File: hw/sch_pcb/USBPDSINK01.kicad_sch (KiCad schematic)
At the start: 51 parts, among them J1 USBC_USB4105-GF-A, J11 WAGO_2604-3102, J2 HEADER_2x05_PARALLEL, J3 HEADER_2x04_PARALLEL, J4 HEADER_2x03_PARALLEL, J5 HEADER_2x01, J6 HEADER_2x07_PARALLEL, M1 HOLE, M2 HOLE, M3 HOLE, M4 HOLE, Q2 IRF7469PbF, U1 STUSB4500QTR, U2 NCP1117-3.3

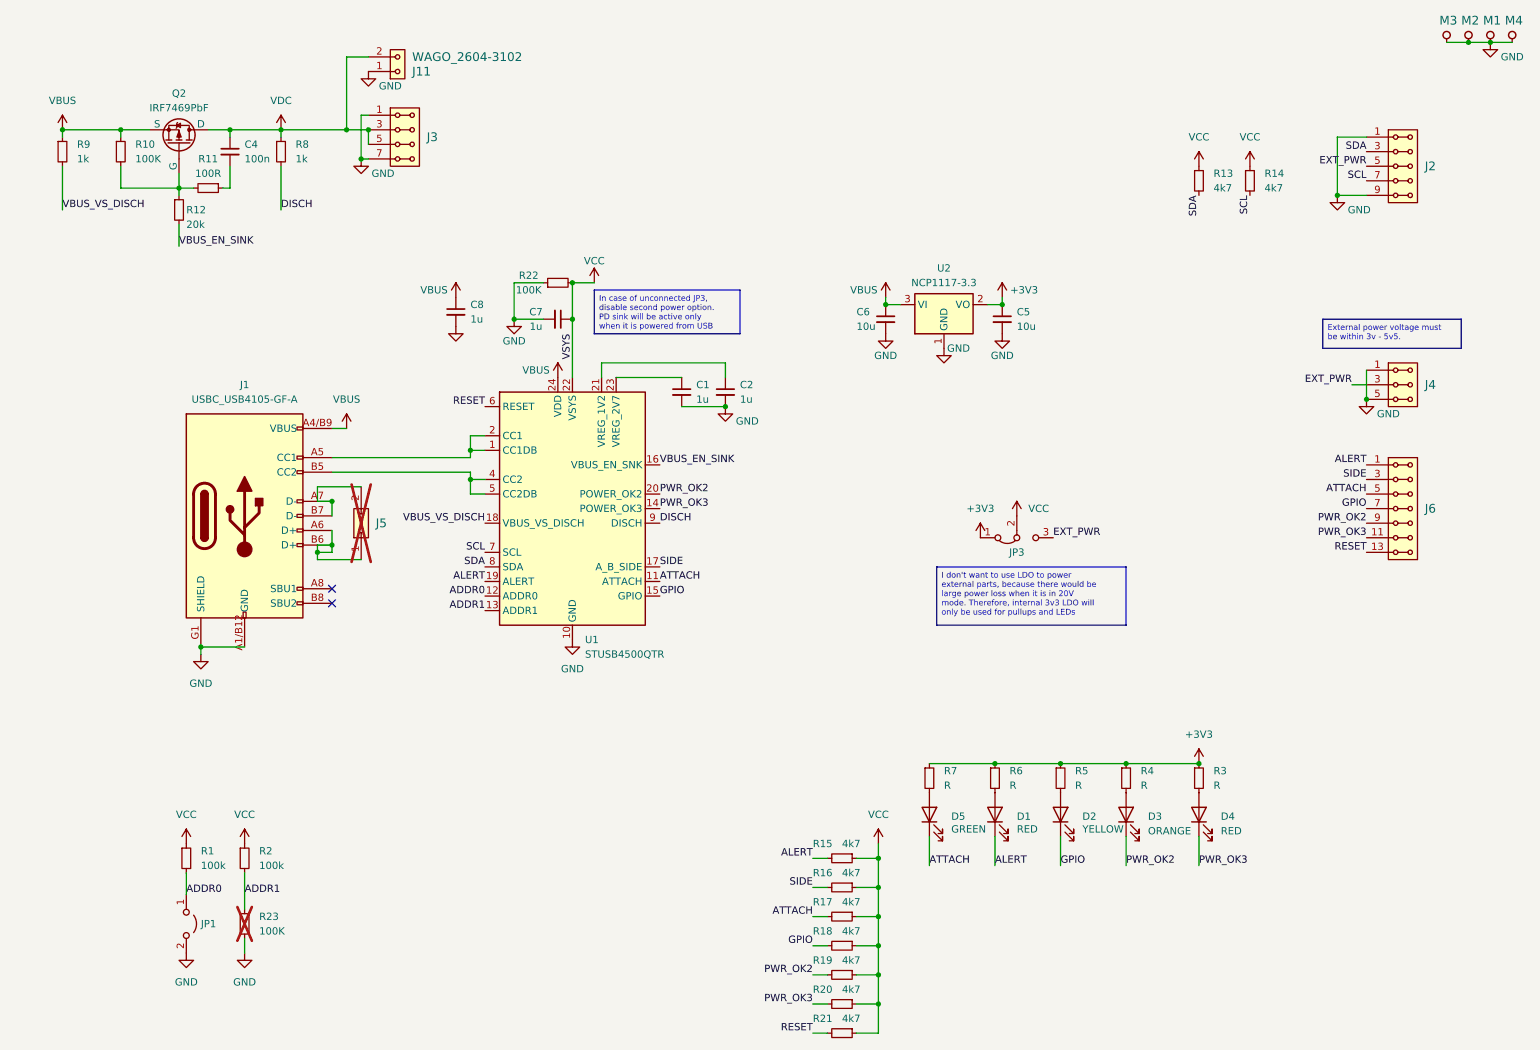
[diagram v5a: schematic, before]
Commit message: minor updates in layout, clean schematics, add components MFPN
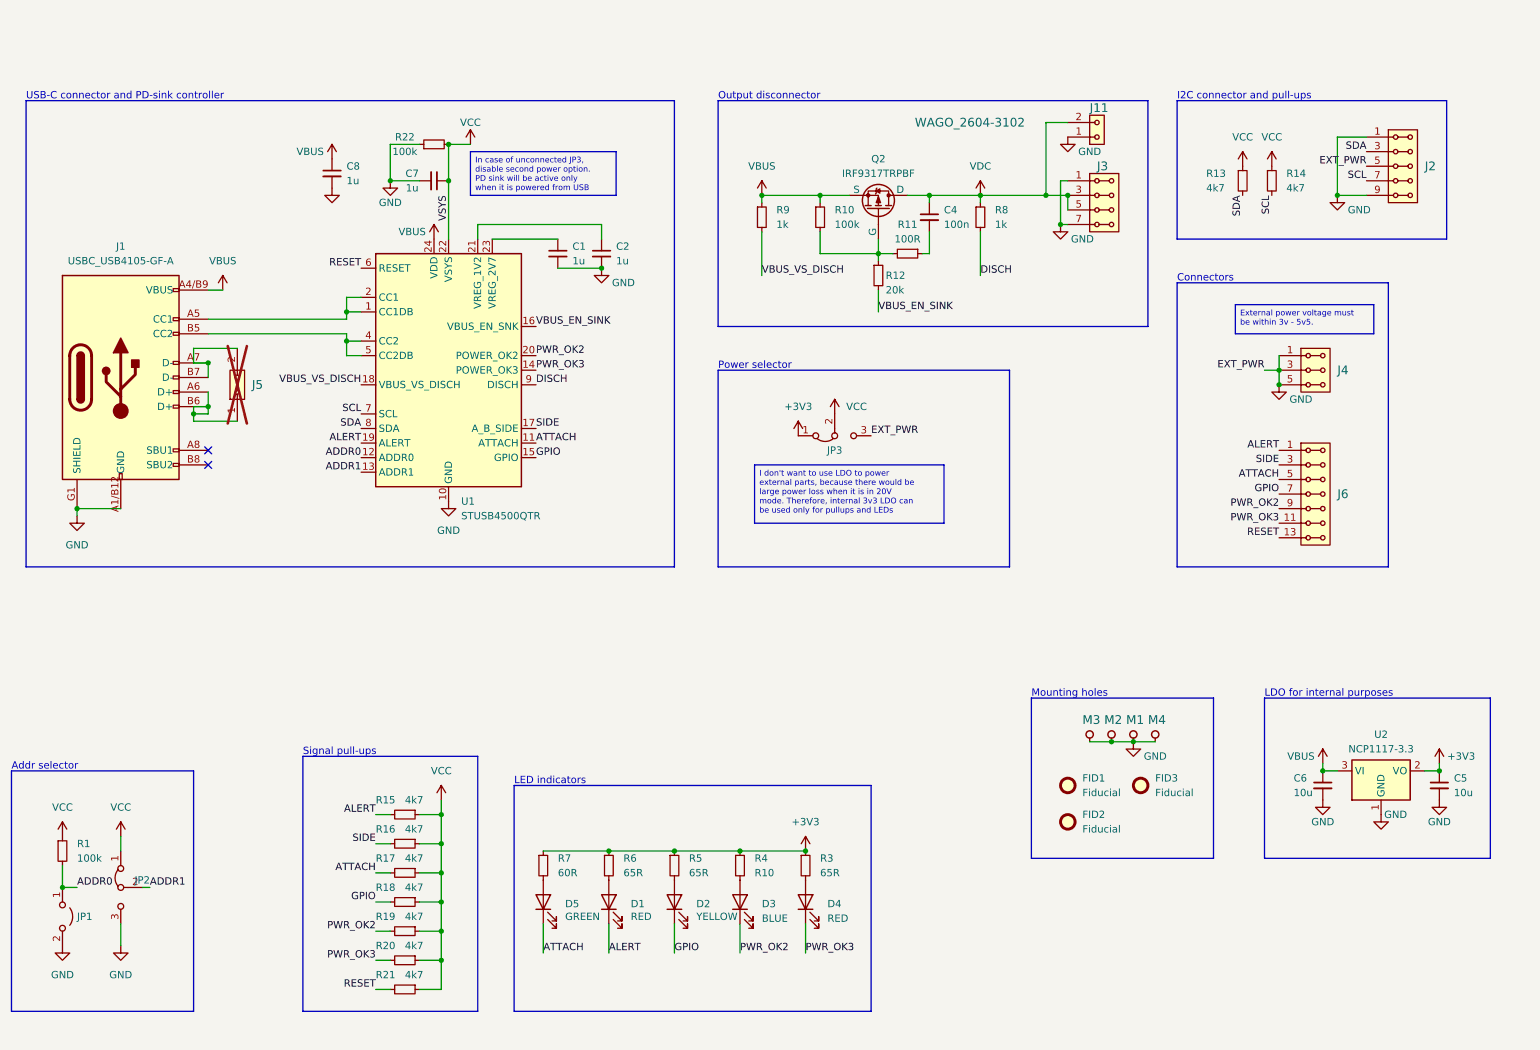
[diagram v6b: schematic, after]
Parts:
- removed R2: 100k, Resistor_SMD:R_0805_2012Metric, symbol Device:R_Small
- removed R23: 100K, Resistor_SMD:R_0805_2012Metric, symbol Device:R_Small
- added FID1, FID2, FID3: Fiducial, Fiducial:Fiducial_1mm_Mask2mm, symbol Mechanical:Fiducial
- added JP2: Jumper_3_Bridged12, Jumper:SolderJumper-3_P1.3mm_Bridged12_RoundedPad1.0x1.5mm, symbol Jumper:Jumper_3_Bridged12
- C1, C2, C7, C8: MFPN (none) -> C0805 1u
- C4: MFPN (none) -> C0805 100n
- C5, C6: MFPN (none) -> C0805 10u
- D1, D4: footprint Mlab_D:LED_1206_2 -> Mlab_D:LED_1206_mill; MFPN (none) -> KPTR-3216SURCK
- D2: footprint Mlab_D:LED_1206_2 -> Mlab_D:LED_1206_mill; MFPN (none) -> KPTR-3216SYCK
- D3: value ORANGE -> BLUE; footprint Mlab_D:LED_1206_2 -> Mlab_D:LED_1206_mill; MFPN (none) -> KPTR-3216QBC-D
- D5: footprint Mlab_D:LED_1206_2 -> Mlab_D:LED_1206_mill; MFPN (none) -> KPTR-3216CGCK
- J1: MFPN (none) -> USB4105-GF-A; UST_ID (none) -> 5fa0f94612875025b397795e
- J11: MFPN (none) -> 2604-3102
- M1, M2, M3, M4: MFPN (none) -> DIN913 M3x12; now left out of the parts list
- Q2: value IRF7469PbF -> IRF9317TRPBF; MFPN (none) -> IRF9317TRPBF; UST_ID (none) -> 64f8de80f3b9d36f37fc9304
- R1: MFPN (none) -> R0805 100K 1%
- R10, R22: value 100K -> 100k; MFPN (none) -> R0805 100K 1%
- R11: MFPN (none) -> R0805 100R 1%
- R12: MFPN (none) -> R0805 20k 1%
- R13, R14, R15, R16, R17, R18, R19, R20, R21: MFPN (none) -> R0805 4k7 1%
- R3, R5, R6: value R -> 65R; MFPN (none) -> R0805 65R 1%
- R4: value R -> R10; MFPN (none) -> R0805 10R 1%
- R7: value R -> 60R; MFPN (none) -> R0805 60R 1%
- R8, R9: MFPN (none) -> R0805 1k 1%
- U1: MFPN (none) -> STUSB4500QTR; UST_ID (none) -> 64f8daa2f3b9d36f37fc92aa
- U2: MFPN (none) -> NCP1117DT33G; UST_ID (none) -> 5c70984712875079b91f8af9
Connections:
- net EXT_PWR is gone; now on net GND: J2.5, J2.6, J4.3, J4.4, JP3.3 (B)
- net ADDR1: now also JP2.2 (C)
- net GND: now also JP2.3 (B)
- net VCC: now also JP2.1 (A)
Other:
- note added: "Addr selector"
- note added: "Connectors"
- note added: "I2C connector and pull-ups"
- note added: "LDO for internal purposes"
- note added: "LED indicators"
- note added: "Mounting holes"
- note added: "Output disconnector"
- note added: "Power selector"
- note added: "Signal pull-ups"
- note added: "USB-C connector and PD-sink controller"
- moved on the sheet: C1, C2, C4, C5, C6, C7, C8, D1, D2, D3, D4, D5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

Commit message: version uploaded to aisler
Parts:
- C1, C2, C7, C8: MPN (none) -> C0805 1u
- C4: MPN (none) -> C0805 100n
- C5, C6: MPN (none) -> C0805 10u
- D1, D4: MPN (none) -> KPTR-3216SURCK
- D2: MPN (none) -> KPTR-3216SYCK
- D3: MPN (none) -> KPTR-3216QBC-D
- D5: MPN (none) -> KPTR-3216CGCK
- J1: MPN (none) -> USB4105-GF-A
- J11: MPN (none) -> 2604-3102
- Q2: MPN (none) -> IRF9317TRPBF
- R1, R10, R22: MPN (none) -> R0805 100K 1%
- R11: MPN (none) -> R0805 100R 1%
- R12: MPN (none) -> R0805 20k 1%
- R13, R14, R15, R16, R17, R18, R19, R20, R21: MPN (none) -> R0805 4k7 1%
- R3, R5, R6: MPN (none) -> R0805 65R 1%
- R4: MPN (none) -> R0805 10R 1%
- R7: MPN (none) -> R0805 60R 1%
- R8, R9: MPN (none) -> R0805 1k 1%
- U1: MPN (none) -> STUSB4500QTR
- U2: MPN (none) -> NCP1117DT33G

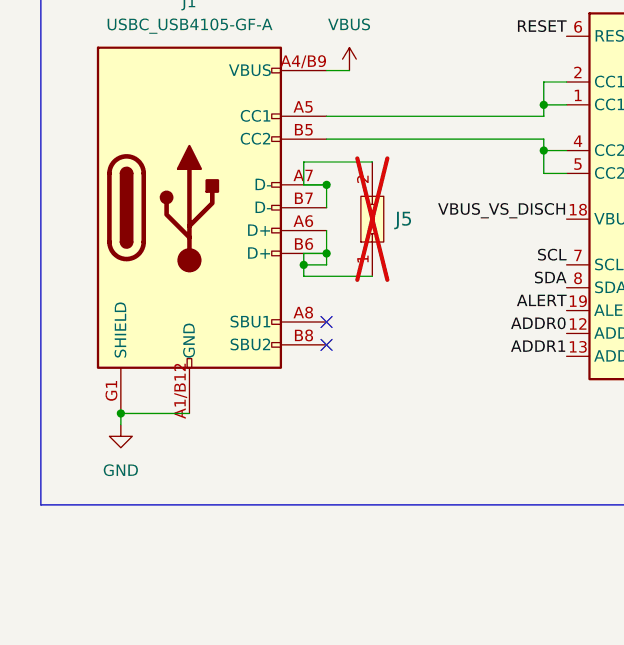
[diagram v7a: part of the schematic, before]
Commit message: Update title block.
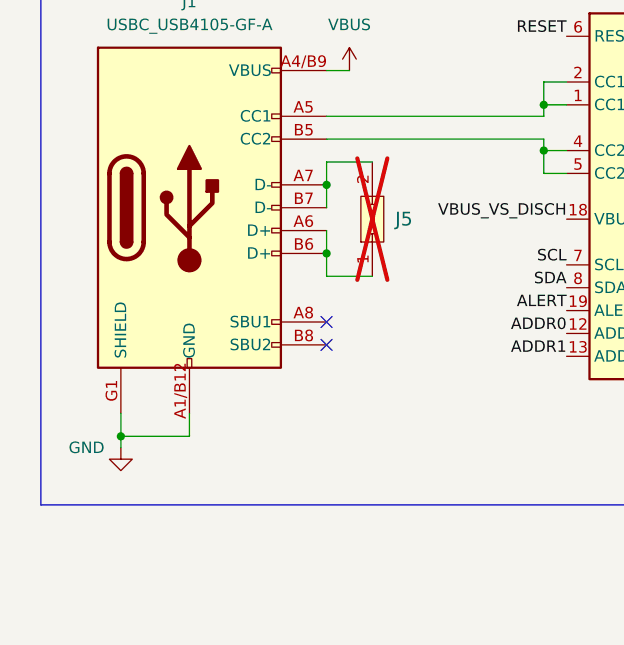
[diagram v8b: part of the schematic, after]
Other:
- company: www.mlab.cz -> roman-dvorak <romandvorak@mlab.cz>
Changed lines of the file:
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@@
   (title_block
     (title "USBPDSINK01A")
-    (company "www.mlab.cz")
+    (company "roman-dvorak <romandvorak@mlab.cz>")
     (comment 1 "USB-C PD sink controller")
-    (comment 2 "roman-dvorak <romandvorak@mlab.cz>")
   )
   (junction (at 156.21 160.02) (diameter 0) (color 0 0 0 0)
@@
   (junction (at 52.07 74.93) (diameter 0) (color 0 0 0 0)
   )
-  (junction (at 29.21 100.33) (diameter 0) (color 0 0 0 0)
+  (junction (at 29.21 102.87) (diameter 0) (color 0 0 0 0)
   )
   (junction (at 266.7 146.05) (diameter 0) (color 0 0 0 0)
@@
   )
   (junction (at 148.59 45.72) (diameter 0) (color 0 0 0 0)
-  )
-  (junction (at 49.53 83.82) (diameter 0) (color 0 0 0 0)
   )
   (junction (at 92.71 163.83) (diameter 0) (color 0 0 0 0)
@@
     (stroke (width 0) (type default))
   )
-  (wire (pts (xy 52.07 82.55) (xy 52.07 83.82))
+  (wire (pts (xy 52.07 82.55) (xy 52.07 85.09))
     (stroke (width 0) (type default))
   )
@@
     (stroke (width 0) (type default))
   )
+  (wire (pts (xy 29.21 102.87) (xy 29.21 100.33))
+    (stroke (width 0) (type default))
+  )
   (wire (pts (xy 93.98 36.83) (xy 93.98 43.18))
     (stroke (width 0) (type default))
@@
     (stroke (width 0) (type default))
   )
-  (wire (pts (xy 29.21 100.33) (xy 29.21 101.6))
+  (wire (pts (xy 29.21 102.87) (xy 29.21 104.14))
     (stroke (width 0) (type default))
   )
@@
     (stroke (width 0) (type default))
   )
+  (wire (pts (xy 36.83 102.87) (xy 36.83 100.33))
+    (stroke (width 0) (type default))
+  )
   (wire (pts (xy 177.8 52.07) (xy 177.8 55.88))
     (stroke (width 0) (type default))
@@
     (stroke (width 0) (type default))
   )
-  (wire (pts (xy 52.07 82.55) (xy 49.53 82.55))
-    (stroke (width 0) (type default))
-  )
   (wire (pts (xy 248.92 45.72) (xy 254 45.72))
     (stroke (width 0) (type default))
@@
     (stroke (width 0) (type default))
   )
-  (wire (pts (xy 49.53 83.82) (xy 49.53 85.09))
-    (stroke (width 0) (type default))
-  )
-  (wire (pts (xy 52.07 74.93) (xy 49.53 74.93))
-    (stroke (width 0) (type default))
-  )
   (wire (pts (xy 177.8 45.72) (xy 186.69 45.72))
     (stroke (width 0) (type default))
@@
     (stroke (width 0) (type default))
   )
-  (wire (pts (xy 52.07 83.82) (xy 49.53 83.82))
-    (stroke (width 0) (type default))
-  )
   (wire (pts (xy 81.28 179.07) (xy 83.82 179.07))
     (stroke (width 0) (type default))
@@
     (stroke (width 0) (type default))
   )
-  (wire (pts (xy 49.53 72.39) (xy 49.53 74.93))
+  (wire (pts (xy 52.07 72.39) (xy 52.07 74.93))
     (stroke (width 0) (type default))
   )
@@
     (stroke (width 0) (type default))
   )
-  (wire (pts (xy 49.53 83.82) (xy 49.53 82.55))
-    (stroke (width 0) (type default))
-  )
   (wire (pts (xy 186.69 52.07) (xy 186.69 59.69))
     (stroke (width 0) (type default))
@@
     (stroke (width 0) (type default))
   )
-  (wire (pts (xy 29.21 100.33) (xy 36.83 100.33))
+  (wire (pts (xy 29.21 102.87) (xy 36.83 102.87))
     (stroke (width 0) (type default))
   )
@@
     (stroke (width 0) (type default))
   )
+  (wire (pts (xy 52.07 85.09) (xy 57.15 85.09))
+    (stroke (width 0) (type default))
+  )
   (wire (pts (xy 144.78 172.72) (xy 144.78 177.8))
     (stroke (width 0) (type default))
@@
     (stroke (width 0) (type default))
   )
-  (wire (pts (xy 49.53 85.09) (xy 57.15 85.09))
-    (stroke (width 0) (type default))
-  )
-  (wire (pts (xy 49.53 72.39) (xy 57.15 72.39))
+  (wire (pts (xy 52.07 72.39) (xy 57.15 72.39))
     (stroke (width 0) (type default))
   )
@@
     )
   )
-  (symbol (lib_id "power:GND") (at 29.21 101.6 0) (unit 1)
-    (in_bom yes) (on_board yes) (dnp no) (fields_autoplaced)
-    (property "Reference" "#PWR02" (at 29.21 107.95 0)
-      (effects (font (size 1.27 1.27)) hide)
-    )
-    (property "Value" "GND" (at 29.21 106.68 0)
-      (effects (font (size 1.27 1.27)))
-    )
-    (property "Footprint" "" (at 29.21 101.6 0)
-      (effects (font (size 1.27 1.27)) hide)
-    )
-    (property "Datasheet" "" (at 29.21 101.6 0)
-      (effects (font (size 1.27 1.27)) hide)
-    )
+  (symbol (lib_id "power:GND") (at 29.21 104.14 0) (unit 1)
+    (in_bom yes) (on_board yes) (dnp no)
+    (property "Reference" "#PWR02" (at 29.21 110.49 0)
+      (effects (font (size 1.27 1.27)) hide)
+    )
+    (property "Value" "GND" (at 25.4 104.14 0)
+      (effects (font (size 1.27 1.27)))
+    )
+    (property "Footprint" "" (at 29.21 104.14 0)
+      (effects (font (size 1.27 1.27)) hide)
+    )
+    (property "Datasheet" "" (at 29.21 104.14 0)
+      (effects (font (size 1.27 1.27)) hide)
+    )
